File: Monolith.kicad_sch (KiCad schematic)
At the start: 20 parts, among them J2 Conn_01x11, J3 Conn_01x11, J4 Conn_01x02, J5 Conn_01x02, J6 Conn_01x07, U1 ADS1299IPAGR, U2 ESP32-S2-MINI-1

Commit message: fix pick and place stuff
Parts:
- C18, C32, C34: LCSC C172735 -> C3011705
- C19: footprint Capacitor_SMD:C_0603_1608Metric -> Capacitor_SMD:C_0805_2012Metric; LCSC C312983 -> C141660
- C20, C35, C36, C37, C38: LCSC C5189821 -> C15849
- R28: LCSC C4231187 -> C105578
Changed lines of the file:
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@@
       (effects (font (size 1.27 1.27)) hide)
     )
-    (property "LCSC" "C5189821" (at 95.25 142.24 0)
+    (property "LCSC" "C15849" (at 95.25 142.24 0)
       (effects (font (size 1.27 1.27)) hide)
     )
@@
       (effects (font (size 1.27 1.27)))
     )
-    (property "Footprint" "Capacitor_SMD:C_0603_1608Metric" (at 146.05 134.9248 0)
+    (property "Footprint" "Capacitor_SMD:C_0805_2012Metric" (at 146.05 134.9248 0)
       (effects (font (size 1.27 1.27)) hide)
     )
@@
       (effects (font (size 1.27 1.27)) hide)
     )
-    (property "LCSC" "C312983" (at 142.24 135.89 90)
+    (property "LCSC" "C141660" (at 142.24 135.89 90)
       (effects (font (size 1.27 1.27)) hide)
     )
@@
       (effects (font (size 1.27 1.27)) hide)
     )
-    (property "LCSC" "C172735" (at 85.09 132.08 0)
+    (property "LCSC" "C3011705" (at 85.09 132.08 0)
       (effects (font (size 1.27 1.27)) hide)
     )
@@
       (effects (font (size 1.27 1.27)) hide)
     )
-    (property "LCSC" "C5189821" (at 144.78 149.86 0)
+    (property "LCSC" "C15849" (at 144.78 149.86 0)
       (effects (font (size 1.27 1.27)) hide)
     )
@@
       (effects (font (size 1.27 1.27)) hide)
     )
-    (property "LCSC" "C5189821" (at 85.09 139.7 0)
+    (property "LCSC" "C15849" (at 85.09 139.7 0)
       (effects (font (size 1.27 1.27)) hide)
     )
@@
       (effects (font (size 1.27 1.27)) hide)
     )
-    (property "LCSC" "C5189821" (at 157.48 149.86 0)
+    (property "LCSC" "C15849" (at 157.48 149.86 0)
       (effects (font (size 1.27 1.27)) hide)
     )
@@
       (effects (font (size 1.27 1.27)) hide)
     )
-    (property "LCSC" "C5189821" (at 155.575 138.43 90)
+    (property "LCSC" "C15849" (at 155.575 138.43 90)
       (effects (font (size 1.27 1.27)) hide)
     )
@@
       (effects (font (size 1.27 1.27)) hide)
     )
-    (property "LCSC" "C172735" (at 209.55 42.545 90)
+    (property "LCSC" "C3011705" (at 209.55 42.545 90)
       (effects (font (size 1.27 1.27)) hide)
     )
@@
       (effects (font (size 1.27 1.27)) hide)
     )
-    (property "LCSC" "C4231187" (at 78.74 46.355 90)
+    (property "LCSC" "C105578" (at 78.74 46.355 90)
       (effects (font (size 1.27 1.27)) hide)
     )
@@
       (effects (font (size 1.27 1.27)) hide)
     )
-    (property "LCSC" "C172735" (at 92.71 116.84 0)
-      (effects (font (size 1.27 1.27)) hide)
-    )
+    (property "LCSC" "C3011705" (at 92.71 116.84 0)
+      (effects (font (size 1.27 1.27)) hide)
+    )

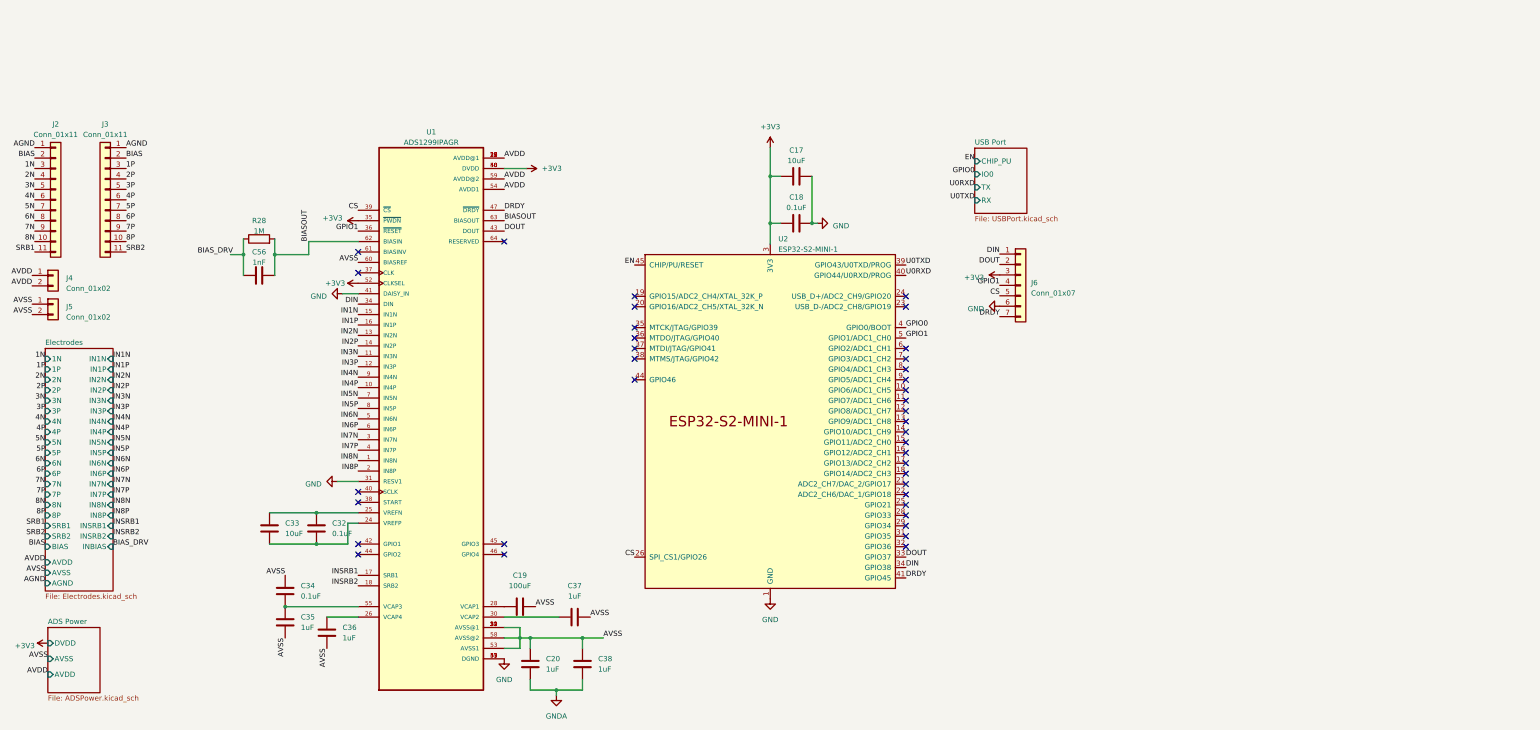
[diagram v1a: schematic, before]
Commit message: Switch out ESP32 for correct model
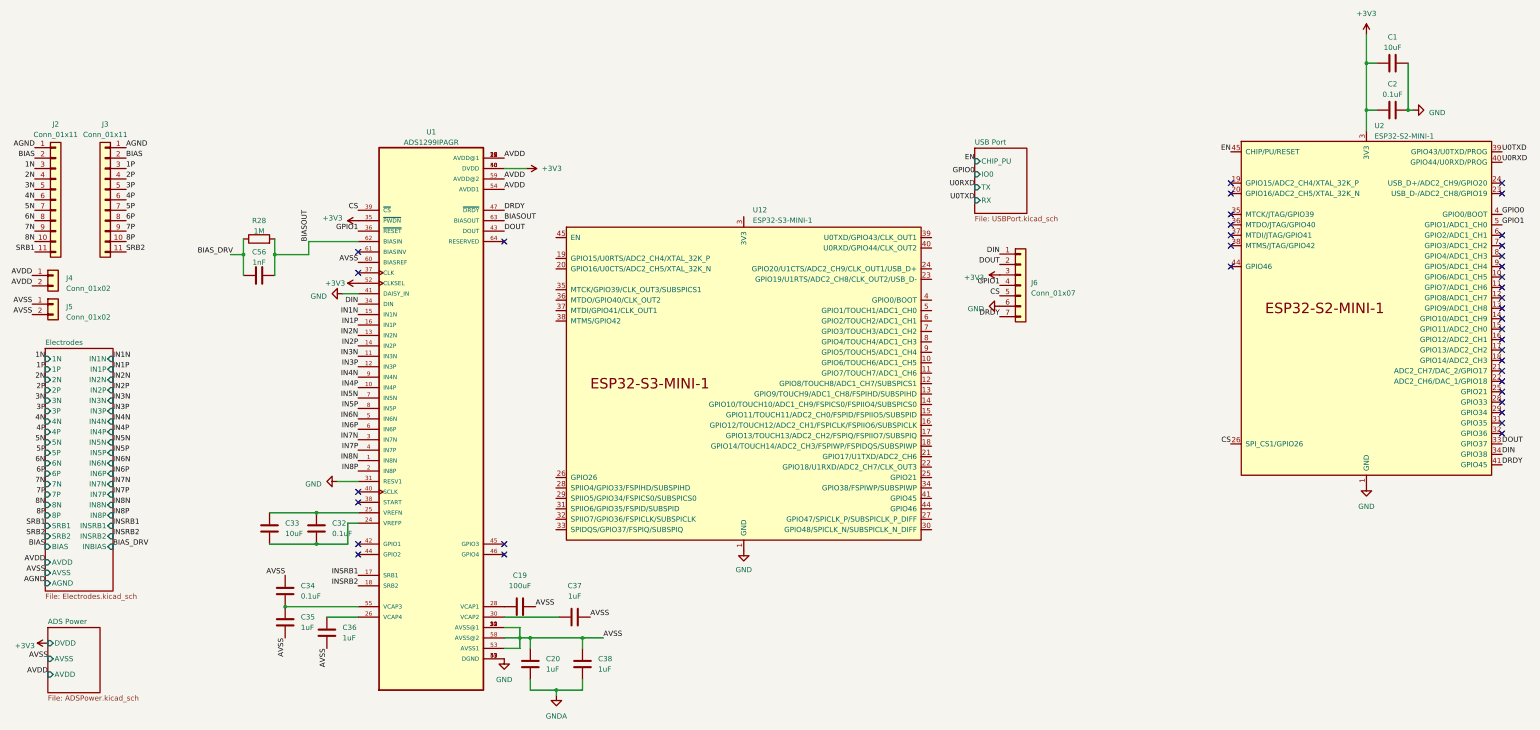
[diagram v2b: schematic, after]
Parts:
- removed C17: 10uF, Capacitor_SMD:C_0603_1608Metric, symbol Device:C
- removed C18: 0.1uF, Capacitor_SMD:C_0603_1608Metric, symbol Device:C
- added C1: 10uF, Capacitor_SMD:C_0603_1608Metric, symbol Device:C
- added C2: 0.1uF, Capacitor_SMD:C_0603_1608Metric, symbol Device:C
- added U12: ESP32-S3-MINI-1, PCM_Espressif:ESP32-S3-MINI-1, symbol PCM_Espressif:ESP32-S3-MINI-1
- U2: footprint PCM_Espressif:ESP32-S2-MINI-1 -> PCM_Espressif:ESP32-S3-MINI-1
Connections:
- net +3V3: now also C1.2, C2.2
- net GND: now also C1.1, C2.1, U12.1 (GND), U12.2 (GND), U12.42 (GND), U12.43 (GND), U12.46 (GND), U12.47 (GND), U12.48 (GND), U12.49 (GND), U12.50 (GND), U12.51 (GND), U12.52 (GND), U12.53 (GND), U12.54 (GND), U12.55 (GND), U12.56 (GND), U12.57 (GND), U12.58 (GND), U12.59 (GND), U12.60 (GND), U12.61 (GND), U12.62 (GND), U12.63 (GND), U12.64 (GND), U12.65 (GND)

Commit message: swap out esp
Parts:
- removed U2: ESP32-S2-MINI-1, PCM_Espressif:ESP32-S3-MINI-1, symbol PCM_Espressif:ESP32-S2-MINI-1
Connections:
- net +3V3: now also U12.3 (3V3)
- net CS: now also U12.14 (GPIO10/TOUCH10/ADC1_CH9/FSPICS0/FSPIIO4/SUBSPICS0)
- net DIN: now also U12.17 (GPIO13/TOUCH13/ADC2_CH2/FSPIQ/FSPIIO7/SUBSPIQ)
- net DOUT: now also U12.15 (GPIO11/TOUCH11/ADC2_CH0/FSPID/FSPIIO5/SUBSPID)
- net DRDY: now also U12.6 (GPIO2/TOUCH2/ADC1_CH1)
- net EN: now also U12.45 (EN)
- net GND: no longer U12.1 (GND), U12.2 (GND), U12.42 (GND), U12.43 (GND), U12.46 (GND), U12.47 (GND), U12.48 (GND), U12.49 (GND), U12.50 (GND), U12.51 (GND), U12.52 (GND), U12.53 (GND), U12.54 (GND), U12.55 (GND), U12.56 (GND), U12.57 (GND), U12.58 (GND), U12.59 (GND), U12.60 (GND), U12.61 (GND), U12.62 (GND), U12.63 (GND), U12.64 (GND), U12.65 (GND)
- net GPIO0: now also U12.4 (GPIO0/BOOT)
- net GPIO1: now also U12.5 (GPIO1/TOUCH1/ADC1_CH0)
- net U0RXD: now also U12.40 (U0RXD/GPIO44/CLK_OUT2)
- net U0TXD: now also U12.39 (U0TXD/GPIO43/CLK_OUT1)
- net SCLK: now reaches U1.40 (SCLK)
- net SCLK: now also U12.16 (GPIO12/TOUCH12/ADC2_CH1/FSPICLK/FSPIIO6/SUBSPICLK)
- new net: U12.1 (GND), U12.2 (GND), U12.42 (GND), U12.43 (GND), U12.46 (GND), U12.47 (GND), U12.48 (GND), U12.49 (GND), U12.50 (GND), U12.51 (GND), U12.52 (GND), U12.53 (GND), U12.54 (GND), U12.55 (GND), U12.56 (GND), U12.57 (GND), U12.58 (GND), U12.59 (GND), U12.60 (GND), U12.61 (GND), U12.62 (GND), U12.63 (GND), U12.64 (GND), U12.65 (GND)
- no-connect marks 38 -> 67
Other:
- moved on the sheet: J6, U12
